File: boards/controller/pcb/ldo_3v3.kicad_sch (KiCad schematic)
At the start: 3 parts, among them U902 NJM2884U1-33-TE1

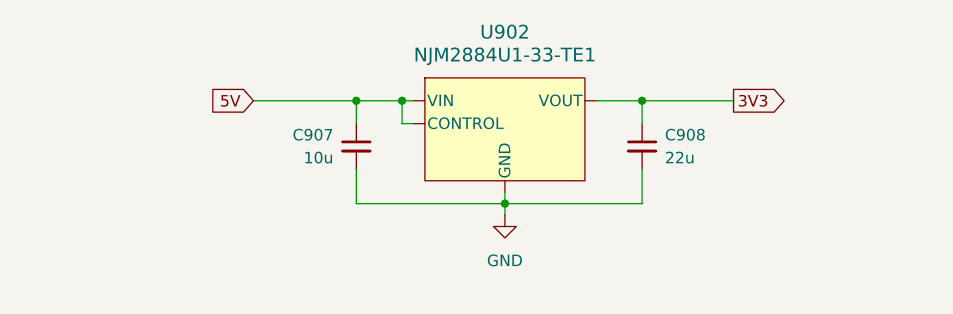
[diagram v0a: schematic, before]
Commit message: controller: pcb: Update schematic
Signed-off-by: Nicholas Loehrke <nicholasnloehrke@gmail.com>
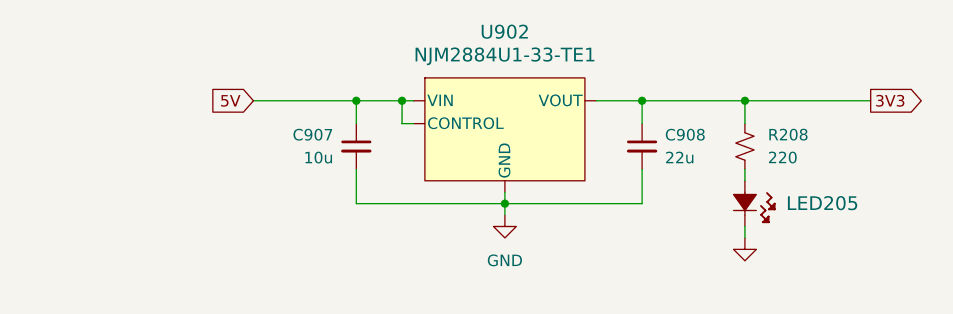
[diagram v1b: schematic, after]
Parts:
- added LED205: B1911PG--20D000514U1930, LED_B1911PG--20D000514U1930_HVK, symbol B1911PG--20D000514U1930:B1911PG--20D000514U1930
- added R208: 220, symbol Device:R_Small_US
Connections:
- net 3V3: now also R208.1
- net GND: now also LED205.1
- new net: LED205.2, R208.2

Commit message: controller: pcb: Update schematic
Signed-off-by: Nicholas Loehrke <nicholasnloehrke@gmail.com>
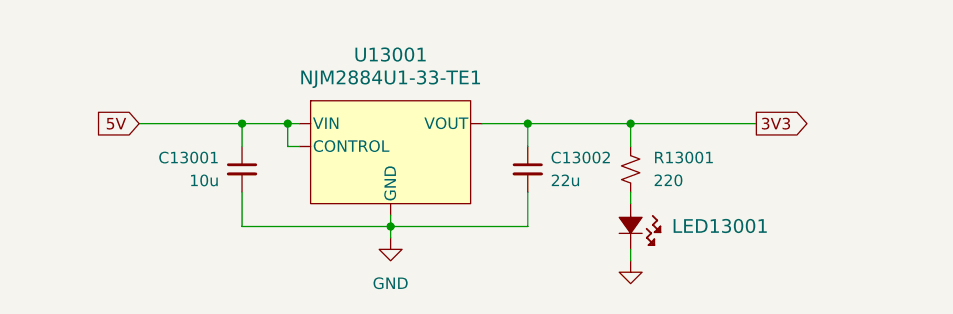
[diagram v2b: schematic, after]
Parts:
- renumbered C907 to C13001, C908 to C13002, LED205 to LED13001, R208 to R13001, U902 to U13001
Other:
- moved on the sheet: C13001, C13002, LED13001, R13001, U13001

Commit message: controller: pcb: Update schematic
Signed-off-by: Nicholas Loehrke <nicholasnloehrke@gmail.com>
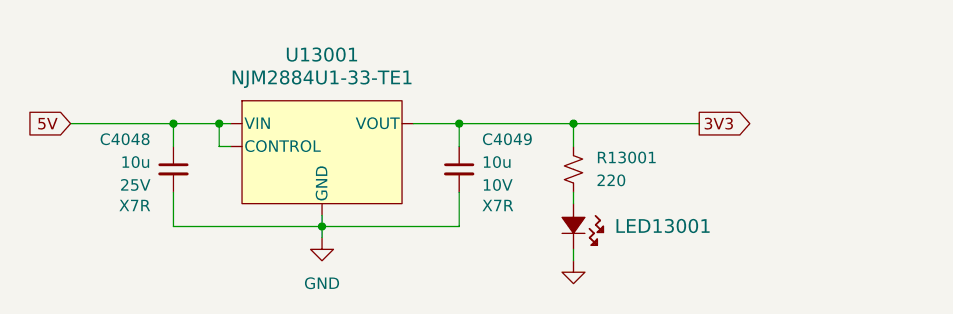
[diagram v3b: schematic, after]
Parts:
- removed C13001: 10u, symbol Device:C_Small
- removed C13002: 22u, symbol Device:C_Small
- added C4048, C4049: 10u, symbol Device:C_Small
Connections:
- net 3V3: now also C4049.1
- net 5V: now also C4048.1
- net GND: now also C4048.2, C4049.2
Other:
- moved on the sheet: LED13001, R13001, U13001

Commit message: controller: pcb: Update schematic
Signed-off-by: Nicholas Loehrke <nicholasnloehrke@gmail.com>
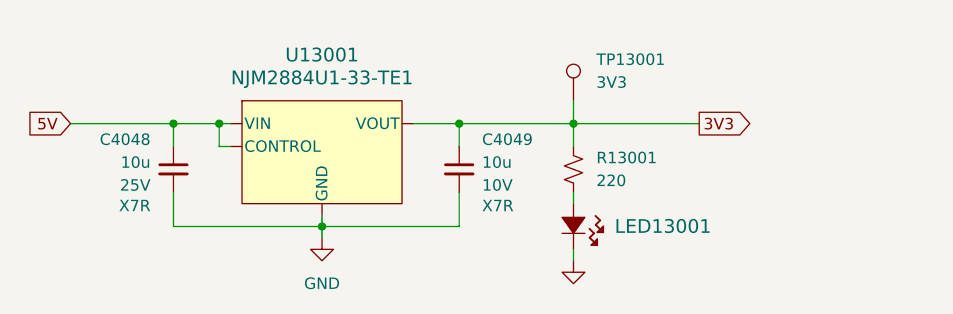
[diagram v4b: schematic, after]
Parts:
- added TP13001: 3V3, symbol Connector:TestPoint
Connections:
- net 3V3: now also TP13001.1
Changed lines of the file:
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@@
+	(wire
+		(pts
+			(xy 167.64 90.17) (xy 167.64 92.71)
+		)
+		(stroke
+			(width 0)
+			(type default)
+		)
+	)
 	(wire
 		(pts
@@
 					(unit 1)
 				)
+			)
+		)
+	)
+	(symbol
+		(lib_id "Connector:TestPoint")
+		(at 167.64 90.17 0)
+		(unit 1)
+		(exclude_from_sim no)
+		(in_bom yes)
+		(on_board yes)
+		(dnp no)
+		(fields_autoplaced yes)
+		(property "Reference" "TP13001"
+			(at 170.18 85.5979 0)
+			(effects
+				(font
+					(size 1.27 1.27)
+				)
+				(justify left)
+			)
+		)
+		(property "Value" "3V3"
+			(at 170.18 88.1379 0)
+			(effects
+				(font
+					(size 1.27 1.27)
+				)
+				(justify left)
+			)
+		)
+		(property "Footprint" ""
+			(at 172.72 90.17 0)
+			(effects
+				(font
+					(size 1.27 1.27)
+				)
+				(hide yes)
+			)
+		)
+		(property "Datasheet" "~"
+			(at 172.72 90.17 0)
+			(effects
+				(font
+					(size 1.27 1.27)
+				)
+				(hide yes)
+			)
+		)
+		(property "Description" "test point"
+			(at 167.64 90.17 0)
+			(effects
+				(font
+					(size 1.27 1.27)
+				)
+				(hide yes)
+			)
+		)
+		(pin "1"
+		)
+		(instances
+			(project ""
+				(path "/5caba13a-97ae-46d4-856f-900b12012fd8/1a4793e5-92d0-4710-847d-f210f4a65056"
+					(reference "TP13001")
+					(unit 1)
+				)

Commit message: controller: pcb: Update schematic + layout
Signed-off-by: Nicholas Loehrke <nicholasnloehrke@gmail.com>
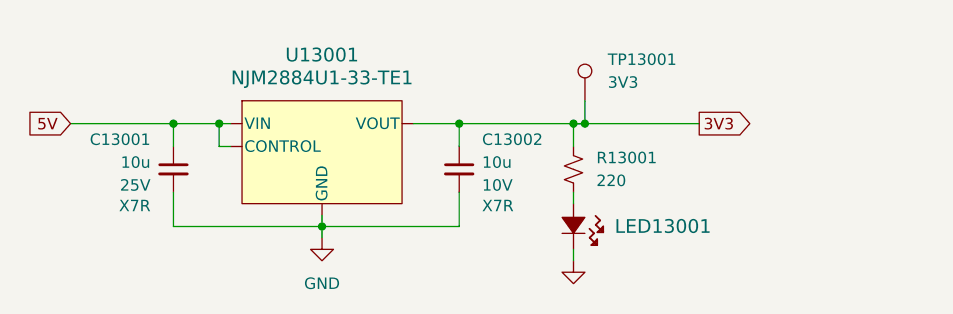
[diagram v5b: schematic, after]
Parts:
- C13001: renamed from C4048; footprint (none) -> Capacitor_SMD:C_1210_3225Metric
- C13002: renamed from C4049; footprint (none) -> Capacitor_SMD:C_1210_3225Metric
- LED13001: footprint LED_B1911PG--20D000514U1930_HVK -> B1911PG--20D000514U1930:B1911PG--20D000514U1930
- R13001: footprint (none) -> Resistor_SMD:R_0603_1608Metric
- TP13001: footprint (none) -> TestPoint:TestPoint_Pad_D1.0mm
- U13001: footprint SOT89-5-1/2_NWJ -> NJM2884U1-33-TE1:NJM2884U1-33-TE1
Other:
- moved on the sheet: TP13001
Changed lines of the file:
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@@
 	(paper "A4")
+	(junction
+		(at 168.91 92.71)
+		(diameter 0)
+		(color 0 0 0 0)
+	)
 	(junction
 		(at 128.27 92.71)
@@
 	(wire
 		(pts
+			(xy 168.91 92.71) (xy 181.61 92.71)
+		)
+		(stroke
+			(width 0.508)
+			(type default)
+		)
+	)
+	(wire
+		(pts
 			(xy 139.7 104.14) (xy 154.94 104.14)
 		)
@@
 	(wire
 		(pts
-			(xy 167.64 90.17) (xy 167.64 92.71)
+			(xy 168.91 90.17) (xy 168.91 92.71)
 		)
 		(stroke
@@
 	(wire
 		(pts
-			(xy 167.64 92.71) (xy 181.61 92.71)
+			(xy 167.64 92.71) (xy 168.91 92.71)
 		)
 		(stroke
@@
 		(stroke
 			(width 0.508)
+			(type default)
+		)
+	)
+	(wire
+		(pts
+			(xy 168.91 92.71) (xy 167.64 92.71)
+		)
+		(stroke
+			(width 0)
 			(type default)
 		)
@@
 			)
 		)
-		(property "Footprint" "LED_B1911PG--20D000514U1930_HVK"
+		(property "Footprint" "B1911PG--20D000514U1930:B1911PG--20D000514U1930"
 			(at 178.054 104.394 0)
 			(effects
@@
 		(on_board yes)
 		(dnp no)
-		(property "Reference" "C4048"
+		(property "Reference" "C13001"
 			(at 120.65 94.488 0)
 			(effects
@@
 			)
 		)
-		(property "Footprint" ""
+		(property "Footprint" "Capacitor_SMD:C_1210_3225Metric"
 			(at 123.19 97.79 0)
 			(effects
@@
 			(project "controller"
 				(path "/5caba13a-97ae-46d4-856f-900b12012fd8/1a4793e5-92d0-4710-847d-f210f4a65056"
-					(reference "C4048")
+					(reference "C13001")
 					(unit 1)
 				)
@@
 	(symbol
 		(lib_id "Connector:TestPoint")
-		(at 167.64 90.17 0)
+		(at 168.91 90.17 0)
 		(unit 1)
 		(exclude_from_sim no)
@@
 		(fields_autoplaced yes)
 		(property "Reference" "TP13001"
-			(at 170.18 85.5979 0)
+			(at 171.45 85.5979 0)
 			(effects
 				(font
@@
 		)
 		(property "Value" "3V3"
-			(at 170.18 88.1379 0)
-			(effects
-				(font
-					(size 1.27 1.27)
-				)
-				(justify left)
-			)
-		)
-		(property "Footprint" ""
-			(at 172.72 90.17 0)
+			(at 171.45 88.1379 0)
+			(effects
+				(font
+					(size 1.27 1.27)
+				)
+				(justify left)
+			)
+		)
+		(property "Footprint" "TestPoint:TestPoint_Pad_D1.0mm"
+			(at 173.99 90.17 0)
 			(effects
 				(font
@@
 		)
 		(property "Datasheet" "~"
-			(at 172.72 90.17 0)
+			(at 173.99 90.17 0)
 			(effects
 				(font
@@
 		)
 		(property "Description" "test point"
-			(at 167.64 90.17 0)
+			(at 168.91 90.17 0)
 			(effects
 				(font
@@
 			)
 		)
-		(property "Footprint" "SOT89-5-1/2_NWJ"
+		(property "Footprint" "NJM2884U1-33-TE1:NJM2884U1-33-TE1"
 			(at 129.794 78.486 0)
 			(effects
@@
 		(on_board yes)
 		(dnp no)
-		(property "Reference" "C4049"
+		(property "Reference" "C13002"
 			(at 157.48 94.488 0)
 			(effects
@@
 			)
 		)
-		(property "Footprint" ""
+		(property "Footprint" "Capacitor_SMD:C_1210_3225Metric"
 			(at 154.94 97.79 0)
 			(effects
@@
 			(project "controller"
 				(path "/5caba13a-97ae-46d4-856f-900b12012fd8/1a4793e5-92d0-4710-847d-f210f4a65056"
-					(reference "C4049")
+					(reference "C13002")
 					(unit 1)
 				)
@@
 			)
 		)
-		(property "Footprint" ""
+		(property "Footprint" "Resistor_SMD:R_0603_1608Metric"
 			(at 167.64 97.79 0)
 			(effects

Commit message: controller: Update BOM
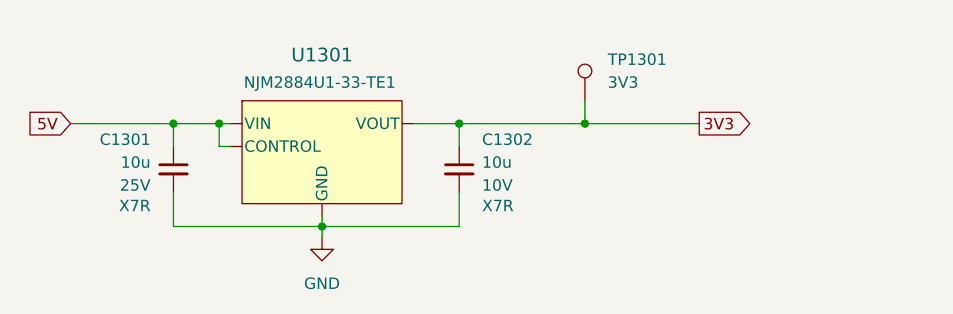
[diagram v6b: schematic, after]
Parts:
- removed LED13001: B1911PG--20D000514U1930, B1911PG--20D000514U1930:B1911PG--20D000514U1930, symbol B1911PG--20D000514U1930:B1911PG--20D000514U1930
- removed R13001: 220, Resistor_SMD:R_0603_1608Metric, symbol Device:R_Small_US
- U1301: renamed from U13001; MPN (none) -> NJM2884U1-33-TE1
- renumbered C13001 to C1301, C13002 to C1302, TP13001 to TP1301
